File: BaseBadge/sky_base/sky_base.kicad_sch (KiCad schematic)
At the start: 12 parts, among them J1 Conn_02x03_Counter_Clockwise, J2 Conn_02x03_Counter_Clockwise

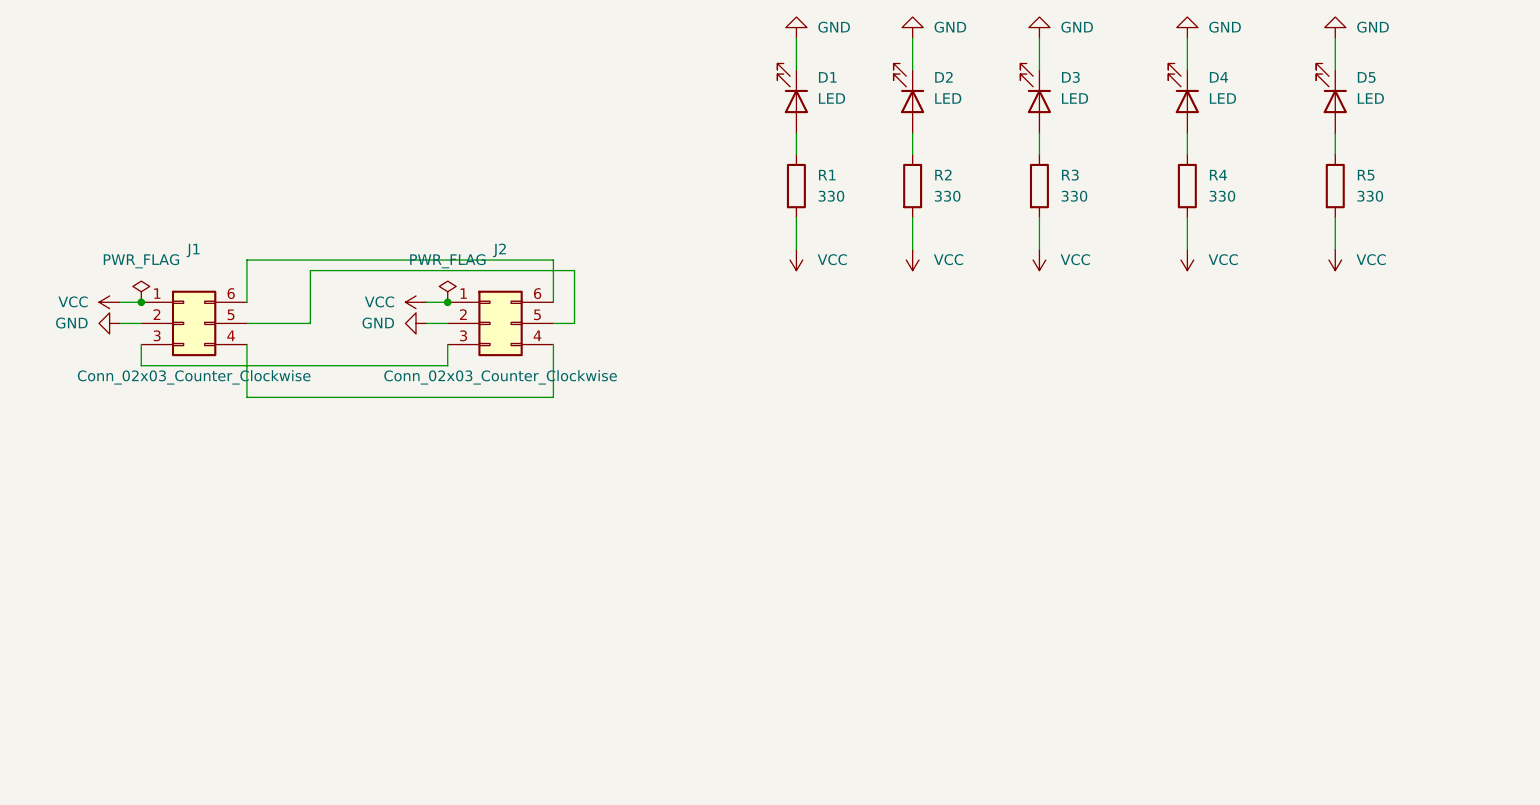
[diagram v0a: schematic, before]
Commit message: overhauls across boards to v02
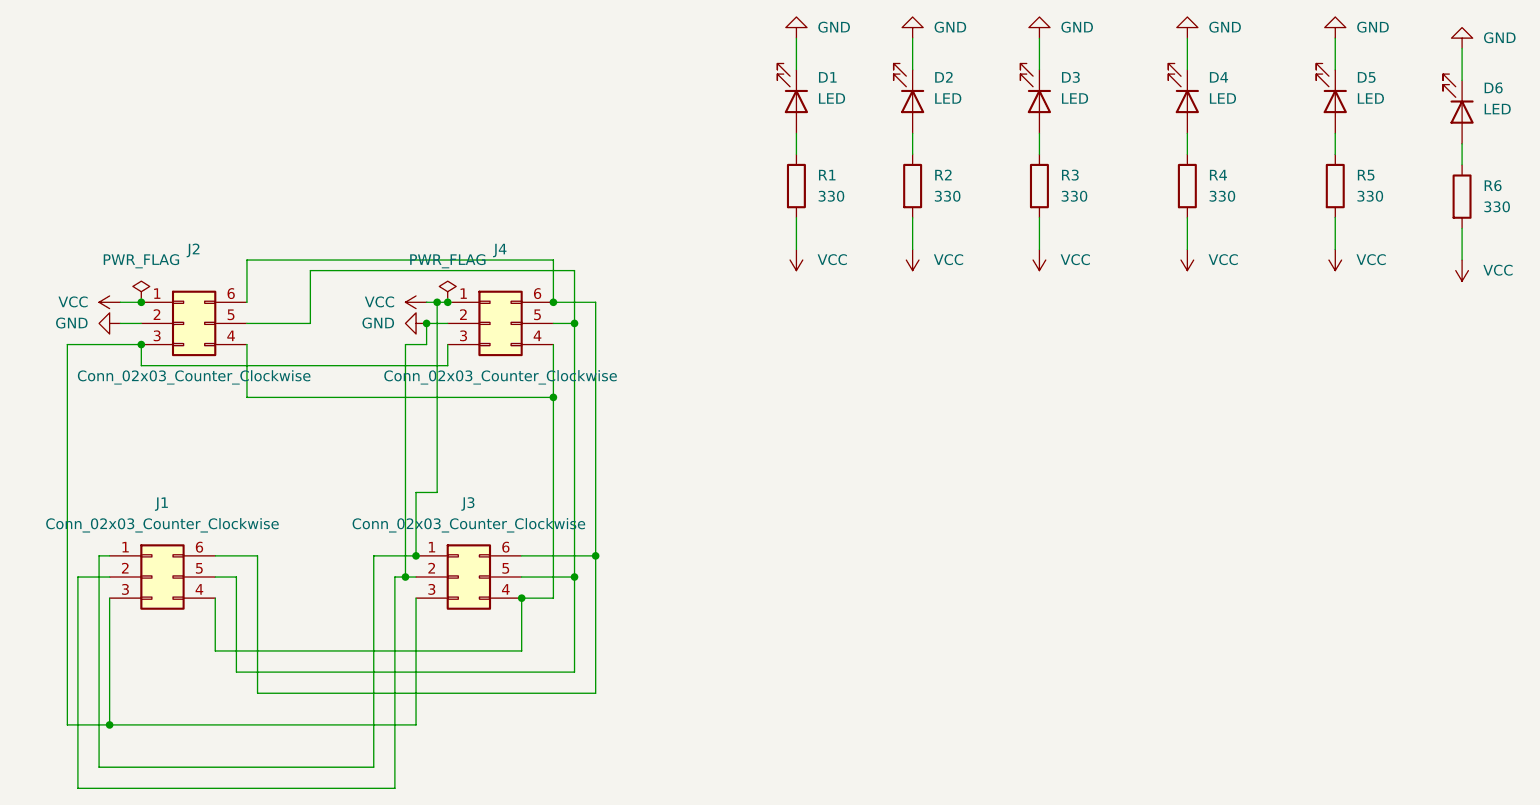
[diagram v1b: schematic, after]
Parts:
- added D6: LED, Base_Library:APTR3216-VFX, symbol Device:LED
- added J1, J3: Conn_02x03_Counter_Clockwise, Connector_PinHeader_2.54mm:PinHeader_2x03_P2.54mm_Vertical, symbol Connector_Generic:Conn_02x03_Counter_Clockwise
- added R6: 330, Resistor_SMD:R_1206_3216Metric_Pad1.30x1.75mm_HandSolder, symbol Device:R
- D1, D2, D3, D4, D5: footprint (none) -> Base_Library:APTR3216-VFX
- J2: renamed from J1; footprint (none) -> Base_Library:space2sky_connector
- J4: renamed from J2; footprint (none) -> Base_Library:sky2ground_connector
- R1, R2, R3, R4, R5: footprint (none) -> Resistor_SMD:R_1206_3216Metric_Pad1.30x1.75mm_HandSolder
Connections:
- net GND: now also D6.1 (K), J1.2 (Pin_2), J3.2 (Pin_2)
- net VCC: now also J1.1 (Pin_1), J3.1 (Pin_1), R6.2
- net at J2.3 (Pin_3), J4.3 (Pin_3): now also J1.3 (Pin_3), J3.3 (Pin_3)
- net at J2.4 (Pin_4), J4.4 (Pin_4): now also J1.4 (Pin_4), J3.4 (Pin_4)
- net at J2.5 (Pin_5), J4.5 (Pin_5): now also J1.5 (Pin_5), J3.5 (Pin_5)
- net at J2.6 (Pin_6), J4.6 (Pin_6): now also J1.6 (Pin_6), J3.6 (Pin_6)
- new net: D6.2 (A), R6.1
